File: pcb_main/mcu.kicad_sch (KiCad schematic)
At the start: 15 parts, among them Q401 2N7002, Q402 2N7002, U401 REF3240, U402 MCP4725, U403 ATmega328P-A, U404 MCP4725

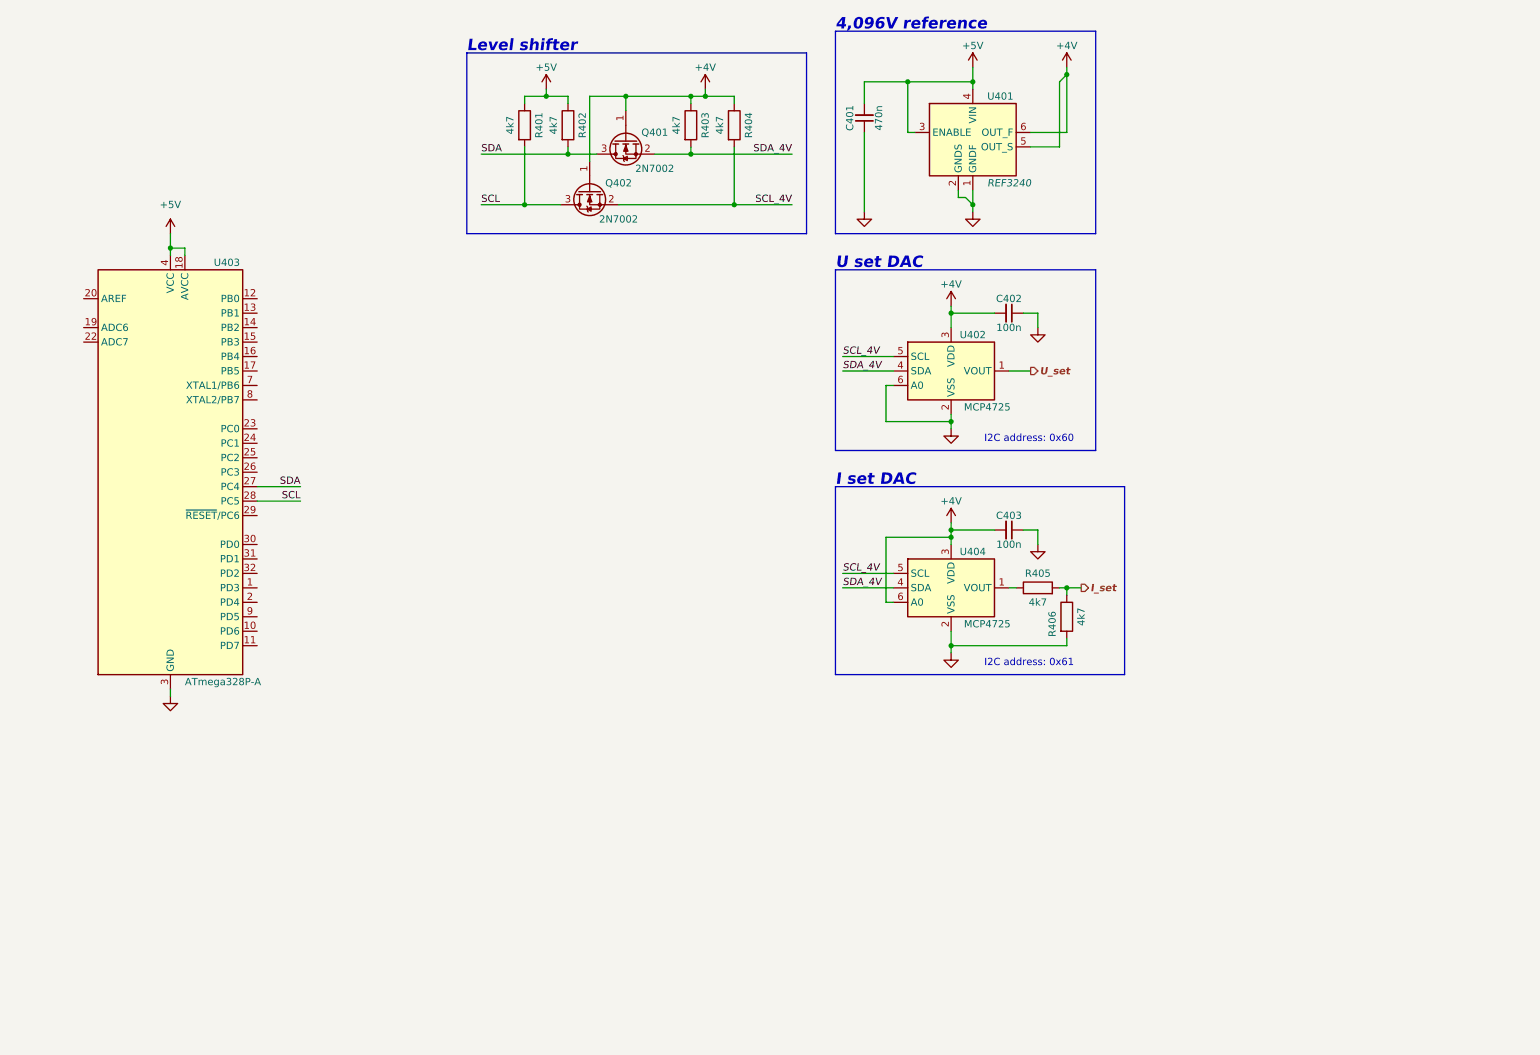
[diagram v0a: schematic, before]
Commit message: power tracks routed
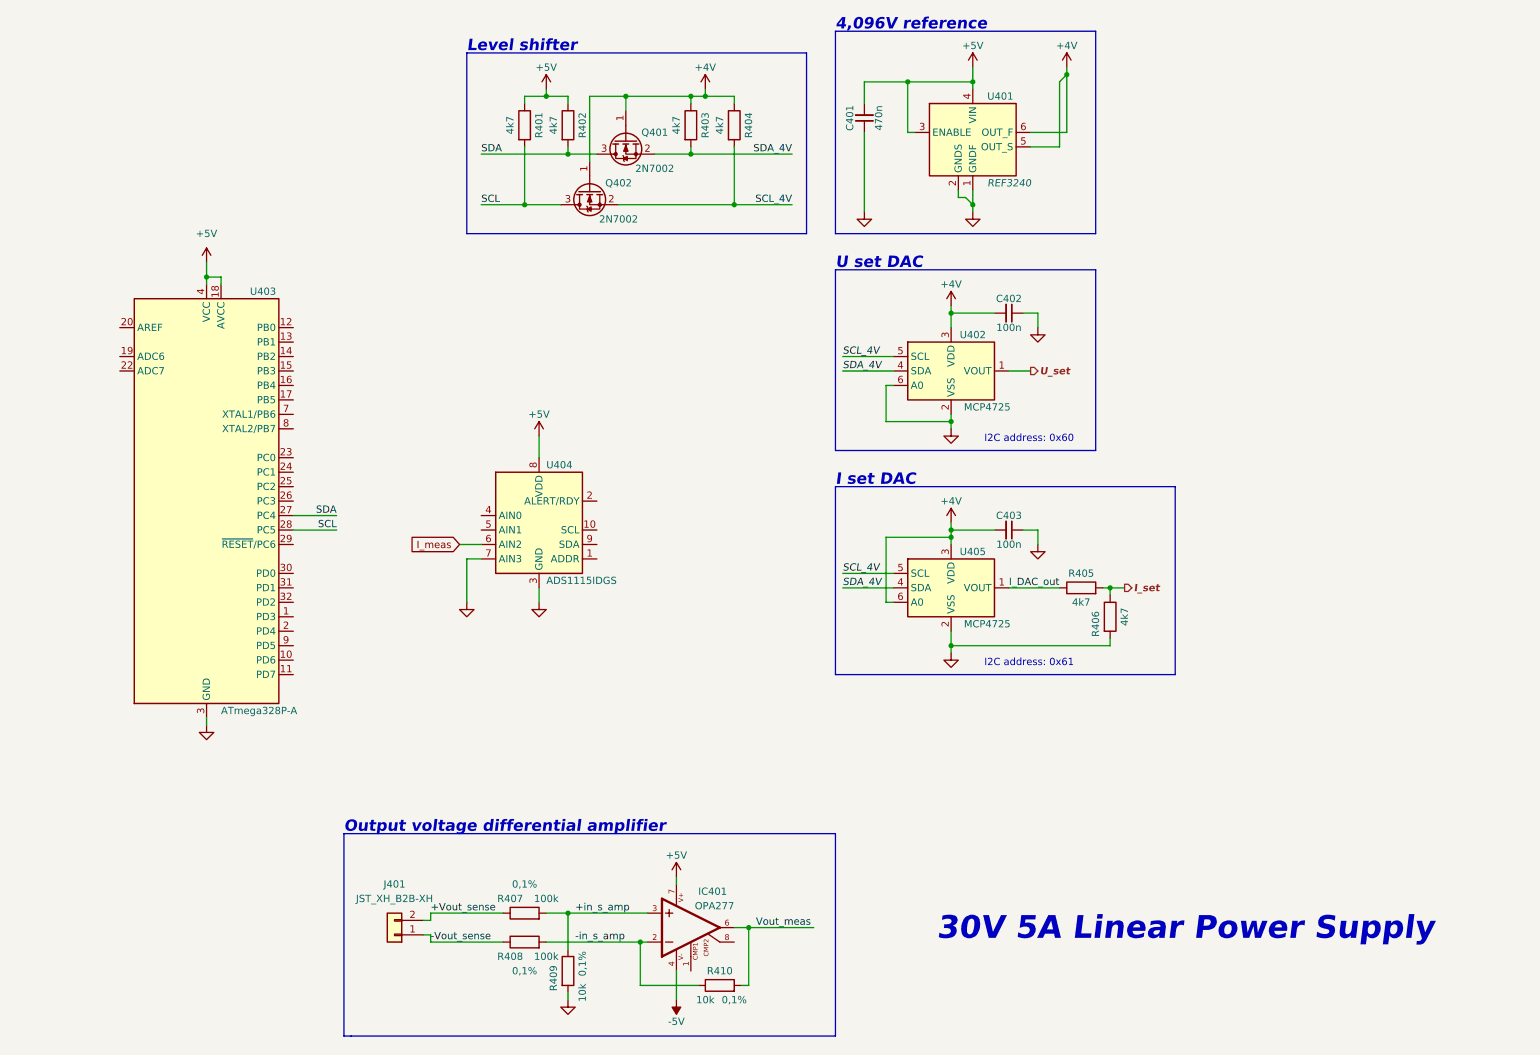
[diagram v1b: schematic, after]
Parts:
- added IC401: OPA277, OPA277:SO08, symbol OPA277:OPA277
- added J401: JST_XH_B2B-XH, Connector_JST:JST_XH_B2B-XH-A_1x02_P2.50mm_Vertical, symbol Connector_Generic:Conn_01x02
- added R407, R408: 100k, Resistor_SMD:R_0603_1608Metric, symbol Device:R
- added R409, R410: 10k, Resistor_SMD:R_0603_1608Metric, symbol Device:R
- added U404: ADS1115IDGS, Package_SO:TSSOP-10_3x3mm_P0.5mm, symbol Analog_ADC:ADS1115IDGS
- renumbered U404 to U405
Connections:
- net +5V: now also IC401.7, U404.8 (VDD)
- net GND: now also R409.2, U404.3 (GND), U404.7 (AIN3)
- net I_DAC_out: now reaches R405.1, U405.1 (VOUT)
- new net +Vout_sense: J401.2 (Pin_2), R407.1
- new net +in_s_amp: IC401.3, R407.2, R409.1
- new net -5V: IC401.4
- new net -Vout_sense: J401.1 (Pin_1), R408.1
- new net -in_s_amp: IC401.2, R408.2, R410.1
- new net I_meas: U404.6 (AIN2)
- new net Vout_meas: IC401.6, R410.2
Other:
- note added: "30V 5A Linear Power Supply"
- note added: "Output voltage differential amplifier"
- company: (none) -> Dominik Workshop
- title: (none) -> MCU + DAC + ADC
- moved on the sheet: R405, R406, U403

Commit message: most layout done
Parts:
- added C404, C405, C408: 100n, Capacitor_SMD:C_0603_1608Metric, symbol Device:C_Small
- added C406, C407: 20p, Capacitor_SMD:C_0603_1608Metric, symbol Device:C_Small
- added J402, J403: JST_XH_B4B-XH, Connector_JST:JST_XH_B4B-XH-A_1x04_P2.50mm_Vertical, symbol Connector_Generic:Conn_01x04
- added J404: Goldpin_2x3, Connector_PinHeader_2.54mm:PinHeader_2x03_P2.54mm_Vertical, symbol Connector_Generic:Conn_02x03_Odd_Even
- added J?: Conn_01x07, Connector_JST:JST_XH_B7B-XH-A_1x07_P2.50mm_Vertical, symbol Connector_Generic:Conn_01x07
- added Y401: 16MHz, Crystal:Crystal_SMD_SeikoEpson_TSX3225-4Pin_3.2x2.5mm, symbol Device:Crystal_GND24_Small
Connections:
- net +5V: now also C404.2, C408.2, J402.1 (Pin_1), J403.1 (Pin_1), J404.2 (Pin_2)
- net -5V: now also C405.1
- net GND: now also U404.1 (ADDR), U404.5 (AIN1), C404.1, C405.2, C406.2, C407.2, C408.1, J402.2 (Pin_2), J403.2 (Pin_2), J404.6 (Pin_6), Y401.2, Y401.4
- net SCL: now also U404.10 (SCL)
- net SDA: now also U404.9 (SDA)
- net Vout_meas: now also U404.4 (AIN0)
- net ADC_RDY: now reaches U404.2 (ALERT/RDY)
- net MOSI: now reaches U403.15 (PB3)
- net MOSI: now also J404.4 (Pin_4)
- net MISO: now reaches U403.16 (PB4)
- net MISO: now also J404.1 (Pin_1)
- net SCK: now reaches U403.17 (PB5)
- net SCK: now also J404.3 (Pin_3)
- net RST: now reaches U403.29 (~{RESET}/PC6)
- net RST: now also J404.5 (Pin_5)
- net XTAL1: now reaches U403.7 (XTAL1/PB6)
- net XTAL1: now also C407.1, Y401.3
- net XTAL2: now reaches U403.8 (XTAL2/PB7)
- net XTAL2: now also C406.1, Y401.1
- new net I_disp_CLK: J403.4 (Pin_4)
- new net I_disp_DIO: J403.3 (Pin_3)
- new net U_disp_CLK: J402.4 (Pin_4)
- new net U_disp_DIO: J402.3 (Pin_3)
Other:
- note added: "ADC"
- note added: "I2C address: 0x48"
- moved on the sheet: C402, C403, IC401, J401, R405, R406, R407, R408, R409, R410, U402, U403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
